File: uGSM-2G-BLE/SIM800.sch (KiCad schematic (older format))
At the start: 1 part

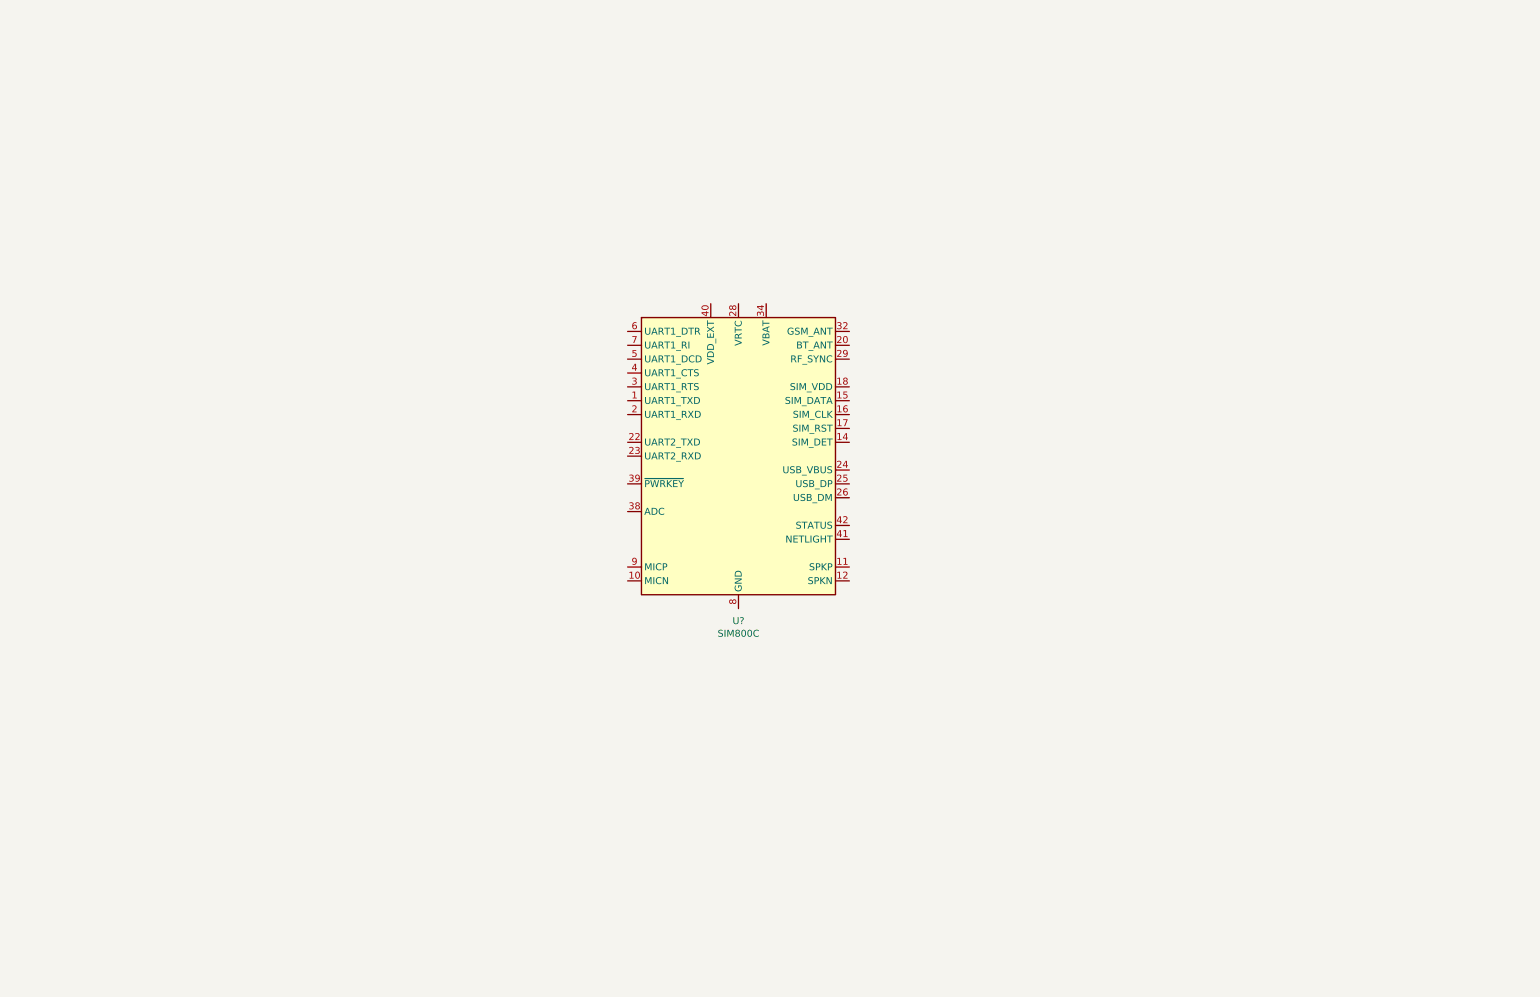
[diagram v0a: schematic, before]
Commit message: added sim800c stuff - needs checking
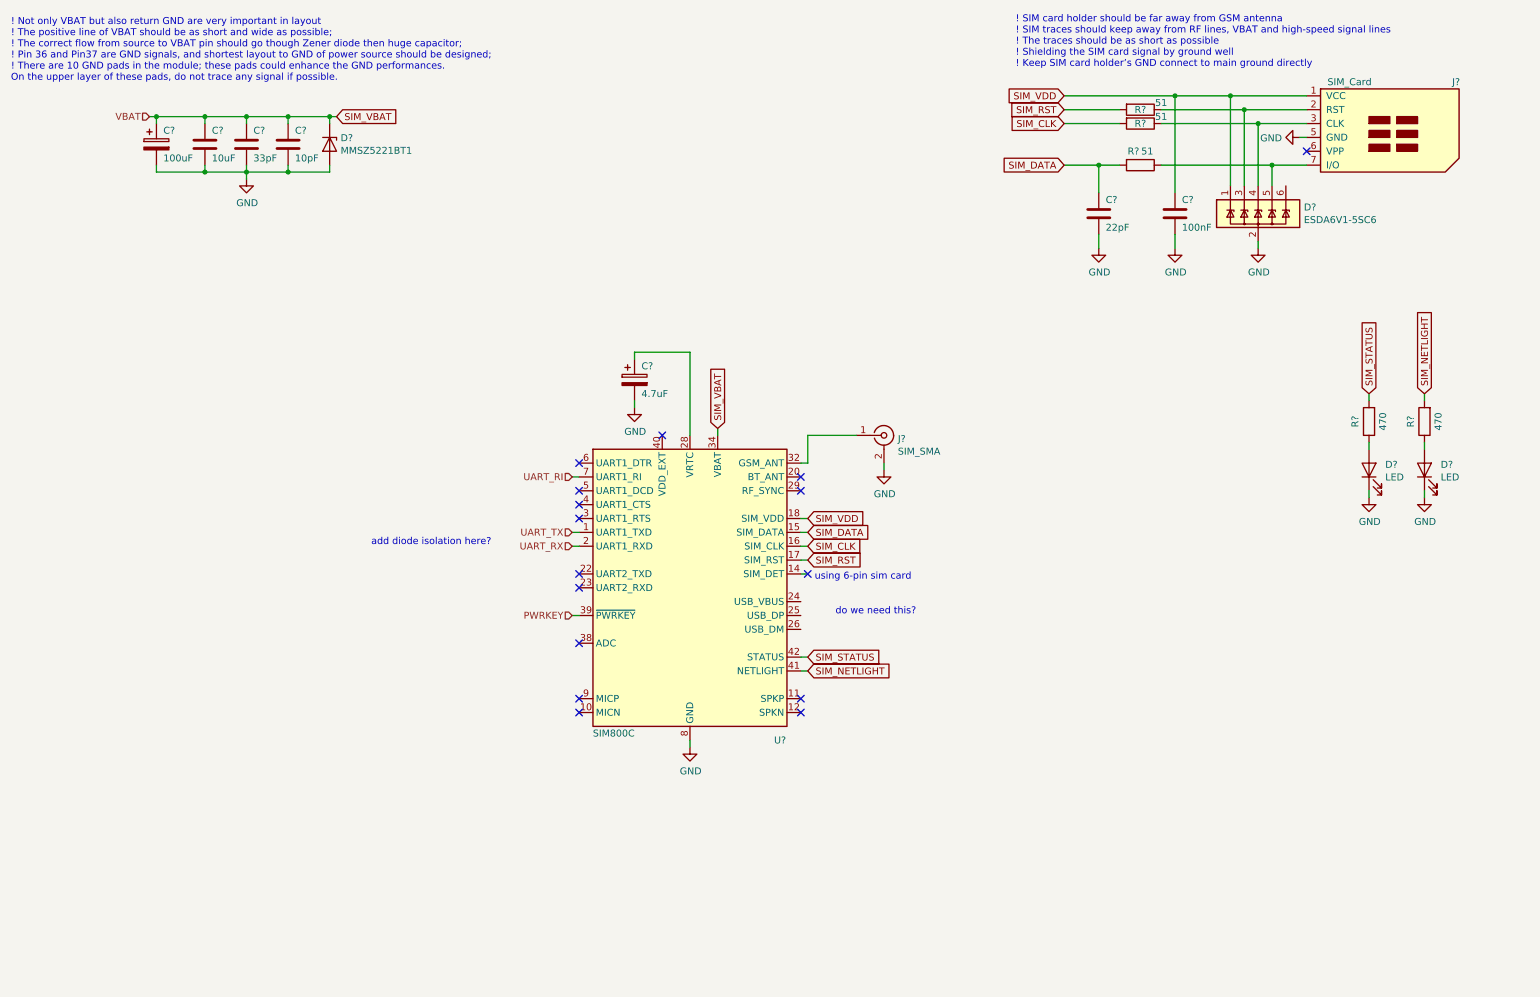
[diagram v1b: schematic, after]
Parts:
- added C?: 100nF, Capacitor_SMD:C_0603_1608Metric, symbol Device:C
- added C?: 22pF, Capacitor_SMD:C_0603_1608Metric, symbol Device:C
- added C?: 100uF, symbol Device:CP
- added C?: 10uF, Capacitor_SMD:C_0603_1608Metric, symbol Device:C
- added C?: 33pF, Capacitor_SMD:C_0603_1608Metric, symbol Device:C
- added C?: 10pF, Capacitor_SMD:C_0603_1608Metric, symbol Device:C
- added C?: 4.7uF, symbol Device:CP
- added D?: ESDA6V1-5SC6, Package_TO_SOT_SMD:SOT-23-6, symbol Power_Protection:ESDA6V1-5SC6
- added D? (x2): LED, LED_SMD:LED_0603_1608Metric, symbol Device:LED
- added D?: MMSZ5221BT1, Diode_SMD:D_SOD-123, symbol Device:D_Zener
- added J?: SIM_SMA, Connector_Coaxial:SMA_Amphenol_132203-12_Horizontal, symbol Connector:Conn_Coaxial
- added J?: SIM_Card, Connector_Card:microSIM_JAE_SF53S006VCBR2000, symbol Connector:SIM_Card
- added R? (x3): 51, Resistor_SMD:R_0603_1608Metric, symbol Device:R
- added R? (x2): 470, Resistor_SMD:R_0603_1608Metric, symbol Device:R
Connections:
- net UART_TX: now reaches U?.1 (UART1_TXD)
- net GND: now reaches U?.13 (GND), U?.19 (GND), U?.21 (GND), U?.27 (GND), U?.30 (GND), U?.31 (GND), U?.33 (GND), U?.36 (GND), U?.37 (GND), U?.8 (GND)
- net GND: now also C?.2, C?.2, C?.2, C?.2, C?.2, C?.2, C?.2, D?.1 (K), D?.1 (K), D?.2 (A), D?.2 (GND), J?.2 (Ext), J?.5 (GND)
- net SIM_DATA: now reaches U?.15 (SIM_DATA)
- net SIM_DATA: now also C?.1, R?.2
- net SIM_CLK: now reaches U?.16 (SIM_CLK)
- net SIM_CLK: now also R?.2
- net SIM_RST: now reaches U?.17 (SIM_RST)
- net SIM_RST: now also R?.2
- net SIM_VDD: now reaches U?.18 (SIM_VDD)
- net SIM_VDD: now also C?.1, D?.1 (IO1), J?.1 (VCC)
- net UART_RX: now reaches U?.2 (UART1_RXD)
- net at U?.28 (VRTC): now also C?.1
- net at U?.32 (GSM_ANT): now also J?.1 (In)
- net SIM_VBAT: now reaches U?.34 (VBAT), U?.35 (VBAT)
- net SIM_VBAT: now also C?.1, C?.1, C?.1, C?.1, D?.1 (K)
- net PWRKEY: now reaches U?.39 (~PWRKEY)
- net SIM_NETLIGHT: now reaches U?.41 (NETLIGHT)
- net SIM_NETLIGHT: now also R?.2
- net SIM_STATUS: now reaches U?.42 (STATUS)
- net SIM_STATUS: now also R?.2
- net UART_RI: now reaches U?.7 (UART1_RI)
- new net: D?.3 (IO2), J?.2 (RST), R?.1
- new net: D?.4 (IO3), J?.3 (CLK), R?.1
- new net: D?.5 (IO4), J?.7 (I/O), R?.1
- new net: D?.2 (A), R?.1 (x2)
- no-connect marks 0 -> 16
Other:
- note added: "! Not only VBAT but also return GND are very important in layout\n! The positive line of VBAT should be as short and wide as possible;\n! The correct flow from source to VBAT pin should go though Zener diode then huge capacitor;\n! Pin 36 and Pin37 are GND signals, and shortest layout to GND of power source should be designed; \n! There are 10 GND pads in the module; these pads could enhance the 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"
- note added: "! SIM card holder should be far away from GSM antenna \n! SIM traces should keep away from RF lines, VBAT and high-speed signal lines\n! The traces should be as short as possible\n! Shielding the SIM card signal by ground well \n! Keep SIM card holder’s GND connect to main ground directly"
- note added: "add diode isolation here?"
- note added: "do we need this?"
- note added: "using 6-pin sim card\n"
- moved on the sheet: U?

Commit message: added all email issue correction
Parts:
- removed D?: LED, LED_SMD:LED_0603_1608Metric, symbol Device:LED
- removed R?: 470, Resistor_SMD:R_0603_1608Metric, symbol Device:R
- added C?: 1uF, Capacitor_SMD:C_0603_1608Metric, symbol Device:C
- added C? (x2): 22pF, Capacitor_SMD:C_0603_1608Metric, symbol Device:C
- added C? (x2): DP, Capacitor_SMD:C_0603_1608Metric, symbol Device:C
- added D?: LED, LED_SMD:LED_0603_1608Metric, symbol Device:LED
- added Q? (x3): MMUN2233LT1G, Package_TO_SOT_SMD:SOT-23, symbol Device:Q_NPN_BEC
- added R? (x2): 22, Resistor_SMD:R_0603_1608Metric, symbol Device:R
- added R?: 470, Resistor_SMD:R_0603_1608Metric, symbol Device:R
- added R?: 0, Resistor_SMD:R_0603_1608Metric, symbol Device:R
- added TP?: SIM_USB_VBUS, TestPoint:TestPoint_Pad_1.0x1.0mm, symbol Connector:TestPoint
- added TP?: SIM_USB_DP, TestPoint:TestPoint_Pad_1.0x1.0mm, symbol Connector:TestPoint
- added TP?: SIM_USB_DM, TestPoint:TestPoint_Pad_1.0x1.0mm, symbol Connector:TestPoint
- added U?: USBLC6, symbol ugsm_lib:USBLC6
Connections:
- net GND: now also C?.2, C?.2, C?.2, C?.2, C?.2, Q?.2 (E), Q?.2 (E), Q?.2 (E), U?.2 (GND); no longer D?.1 (K)
- net PWRKEY: now also Q?.1 (B); no longer U?.39 (~PWRKEY)
- net SIM_CLK: now also C?.1
- net SIM_NETLIGHT: now also Q?.1 (B)
- net SIM_RST: now also C?.1
- net SIM_STATUS: now also Q?.1 (B); no longer R?.2
- net SIM_VBAT: now also D?.2 (A), D?.2 (A)
- net at U?.24 (USB_VBUS): now also C?.1, TP?.1, U?.5 (VCC)
- net at U?.25 (USB_DP): now also R?.2
- net at U?.26 (USB_DM): now also R?.2
- net at U?.32 (GSM_ANT): now also C?.1, R?.2; no longer J?.1 (In)
- net at R?.1: now also Q?.3 (C); no longer D?.2 (A)
- new net: Q?.3 (C), U?.39 (~PWRKEY)
- new net: C?.1, J?.1 (In), R?.1
- new net: D?.1 (K), R?.2 (x2)
- new net: TP?.1, U?.6 (OUTPUT1)
- new net: TP?.1, U?.4 (OUTPUT2)
- new net: R?.1, U?.1 (INPUT1)
- new net: R?.1, U?.3 (INPUT2)
- new net: Q?.3 (C), R?.1
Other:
- note removed: "add diode isolation here?"
- note removed: "do we need this?"
- moved on the sheet: D?, J?, R?

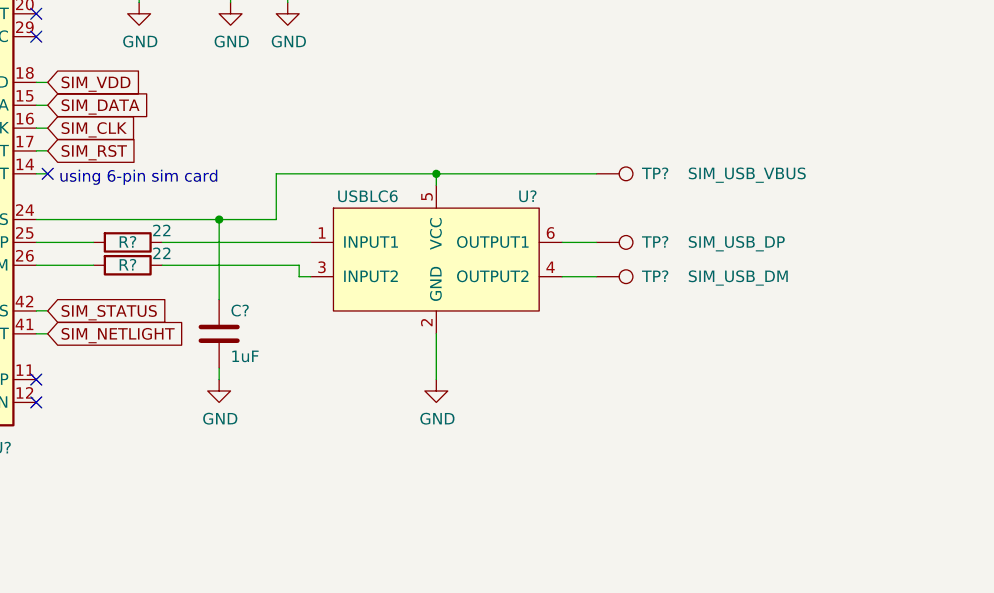
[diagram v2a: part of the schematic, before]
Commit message: removed usbl6 simcom
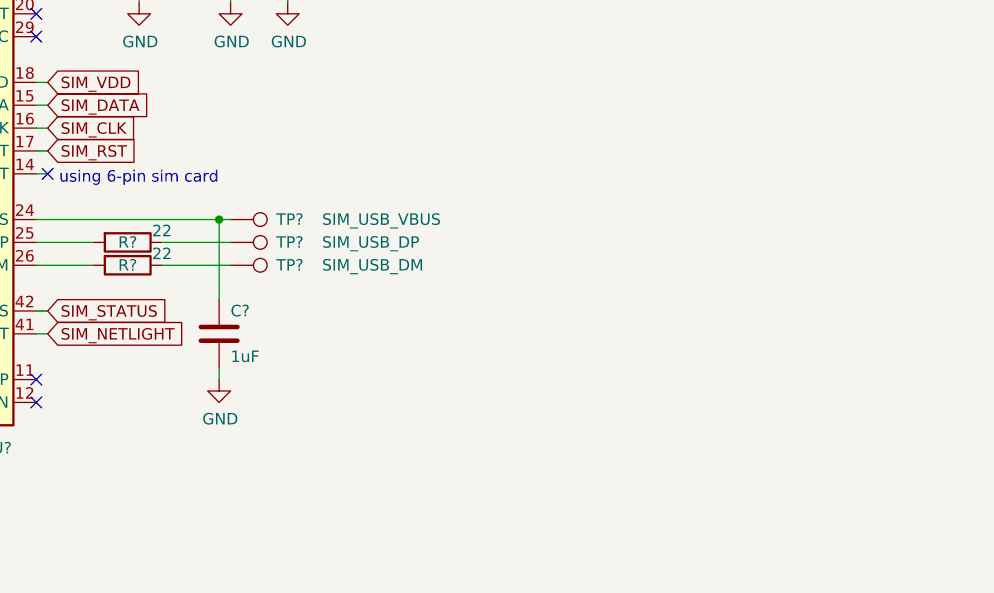
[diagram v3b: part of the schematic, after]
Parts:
- removed U?: USBLC6, symbol ugsm_lib:USBLC6
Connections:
- net at TP?.1: now also R?.1 (x2)
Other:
- moved on the sheet: TP?
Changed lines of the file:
@@
 L Connector:TestPoint TP?
 U 1 1 5E6CAF7A
-P 8750 5100
-F 0 "TP?" V 8750 5300 50  0000 L CNN
-F 1 "SIM_USB_DM" V 8750 5500 50  0000 L CNN
-F 2 "TestPoint:TestPoint_Pad_1.0x1.0mm" H 8950 5100 50  0001 C CNN
-F 3 "~" H 8950 5100 50  0001 C CNN
-	1    8750 5100
+P 7150 5050
+F 0 "TP?" V 7150 5250 50  0000 L CNN
+F 1 "SIM_USB_DM" V 7150 5450 50  0000 L CNN
+F 2 "TestPoint:TestPoint_Pad_1.0x1.0mm" H 7350 5050 50  0001 C CNN
+F 3 "~" H 7350 5050 50  0001 C CNN
+	1    7150 5050
 	0    1    1    0
 $EndComp
@@
 L Connector:TestPoint TP?
 U 1 1 5E6CACB2
-P 8750 4950
-F 0 "TP?" V 8750 5150 50  0000 L CNN
-F 1 "SIM_USB_DP" V 8750 5350 50  0000 L CNN
-F 2 "TestPoint:TestPoint_Pad_1.0x1.0mm" H 8950 4950 50  0001 C CNN
-F 3 "~" H 8950 4950 50  0001 C CNN
-	1    8750 4950
+P 7150 4950
+F 0 "TP?" V 7150 5150 50  0000 L CNN
+F 1 "SIM_USB_DP" V 7150 5350 50  0000 L CNN
+F 2 "TestPoint:TestPoint_Pad_1.0x1.0mm" H 7350 4950 50  0001 C CNN
+F 3 "~" H 7350 4950 50  0001 C CNN
+	1    7150 4950
 	0    1    1    0
 $EndComp
@@
 L Connector:TestPoint TP?
 U 1 1 5E6C7717
-P 8750 4650
-F 0 "TP?" V 8750 4850 50  0000 L CNN
-F 1 "SIM_USB_VBUS" V 8750 5050 50  0000 L CNN
-F 2 "TestPoint:TestPoint_Pad_1.0x1.0mm" H 8950 4650 50  0001 C CNN
-F 3 "~" H 8950 4650 50  0001 C CNN
-	1    8750 4650
+P 7150 4850
+F 0 "TP?" V 7150 5050 50  0000 L CNN
+F 1 "SIM_USB_VBUS" V 7150 5250 50  0000 L CNN
+F 2 "TestPoint:TestPoint_Pad_1.0x1.0mm" H 7350 4850 50  0001 C CNN
+F 3 "~" H 7350 4850 50  0001 C CNN
+	1    7150 4850
 	0    1    1    0
 $EndComp
-$Comp
-L ugsm_lib:USBLC6 U?
-U 1 1 5E770D9A
-P 8050 5050
-F 0 "U?" H 8450 5350 50  0000 C CNN
-F 1 "USBLC6" H 7750 5350 50  0000 C CNN
-F 2 "" H 7800 5250 50  0001 C CNN
-F 3 "" H 7800 5250 50  0001 C CNN
-	1    8050 5050
-	1    0    0    -1
-$EndComp
-Wire Wire Line
-	8750 4650 8050 4650
-Wire Wire Line
-	7350 4650 7350 4850
-Wire Wire Line
-	7350 4850 7100 4850
-Connection ~ 7100 4850
-Wire Wire Line
-	8050 4700 8050 4650
-Connection ~ 8050 4650
-Wire Wire Line
-	8050 4650 7350 4650
-Wire Wire Line
-	6850 4950 7500 4950
-Wire Wire Line
-	6850 5050 7450 5050
-Wire Wire Line
-	7450 5050 7450 5100
-Wire Wire Line
-	7450 5100 7500 5100
-Wire Wire Line
-	8600 4950 8750 4950
-Wire Wire Line
-	8600 5100 8750 5100
-$Comp
-L power:GND #PWR?
-U 1 1 5E78E735
-P 8050 5550
-F 0 "#PWR?" H 8050 5300 50  0001 C CNN
-F 1 "GND" H 8055 5377 50  0000 C CNN
-F 2 "" H 8050 5550 50  0001 C CNN
-F 3 "" H 8050 5550 50  0001 C CNN
-	1    8050 5550
-	1    0    0    -1
-$EndComp
-Wire Wire Line
-	8050 5350 8050 5550
 $Comp
 L Device:C C?
@@
 Wire Wire Line
 	7400 3700 7400 3900
+Wire Wire Line
+	7100 4850 7150 4850
+Connection ~ 7100 4850
+Wire Wire Line
+	6850 4950 7150 4950
+Wire Wire Line
+	6850 5050 7150 5050
 $EndSCHEMATC
